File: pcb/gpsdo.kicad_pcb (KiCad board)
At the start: 4 copper layers, 140 x 100 mm, 163 parts, among them IC1 ICE40LP384-SG32, J1 JTAG, J10 CLK0, J11 CLK7, J12 USB_B_Micro, J13 CLK6, J14 CLK5, J15 CLK4, J16 RF_Shield_One_Piece, J2 SSD1306, J3 EXT_CLOCK, J4 GPS_ANT, J5 USB_B_Micro, J6 CLK3, J7 Screw_Terminal_01x03, J8 CLK2, J9 CLK1, M1 E73-2G4M08S1C-52840, Q1 S9018, SW1 EC11, SW2 MCML4-112B, U1 MCP9808_MSOP, U2 MCP9808_MSOP, U3 TPS652510, U4 LT1763xS8, U5 74LVC1G17, U6 Si5351C-B-GM, U7 74LVC1G17, U8 uBlox NEO-7M, U9 AD5761R, Y1 32768, Y2 8663-XS

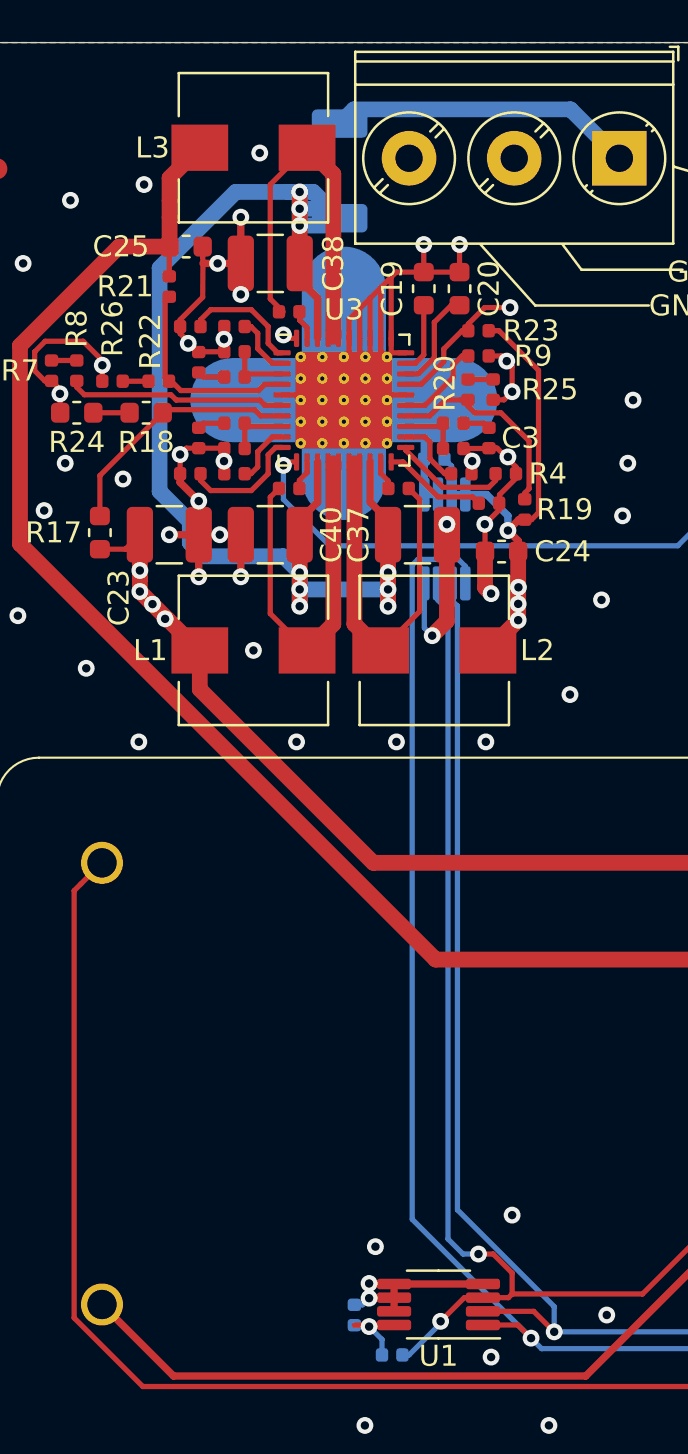
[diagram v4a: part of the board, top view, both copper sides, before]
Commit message: fix L3 to decrease ripple on 1V2 rail
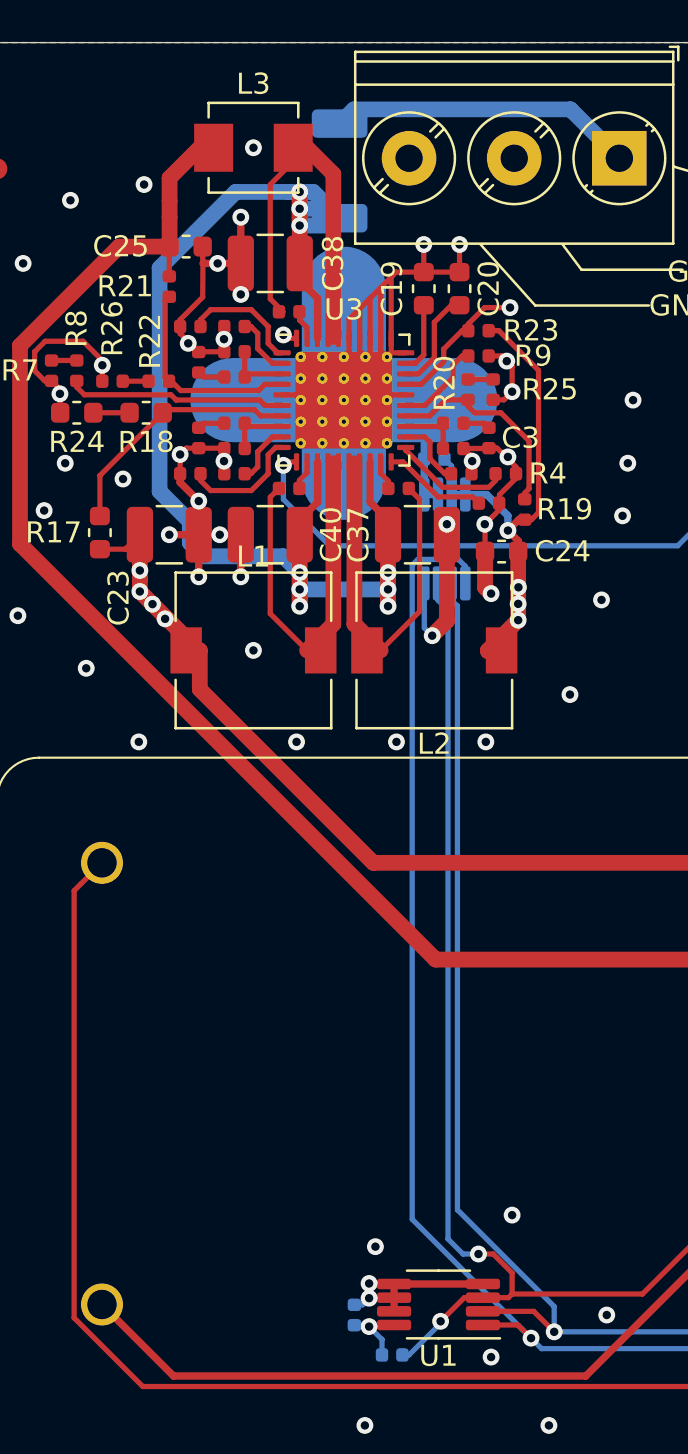
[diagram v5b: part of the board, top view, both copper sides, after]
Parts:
- L1, L2: footprint Inductor_SMD:L_Wuerth_HCI-7050 -> Inductor_SMD:L_7.3x7.3_H4.5
- L3: value 4u7 -> 220u; footprint Inductor_SMD:L_Wuerth_HCI-7050 -> Inductor_SMD:L_Vishay_IHLP-1616
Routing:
- net +3V3: track 79.4 -> 78.7 mm

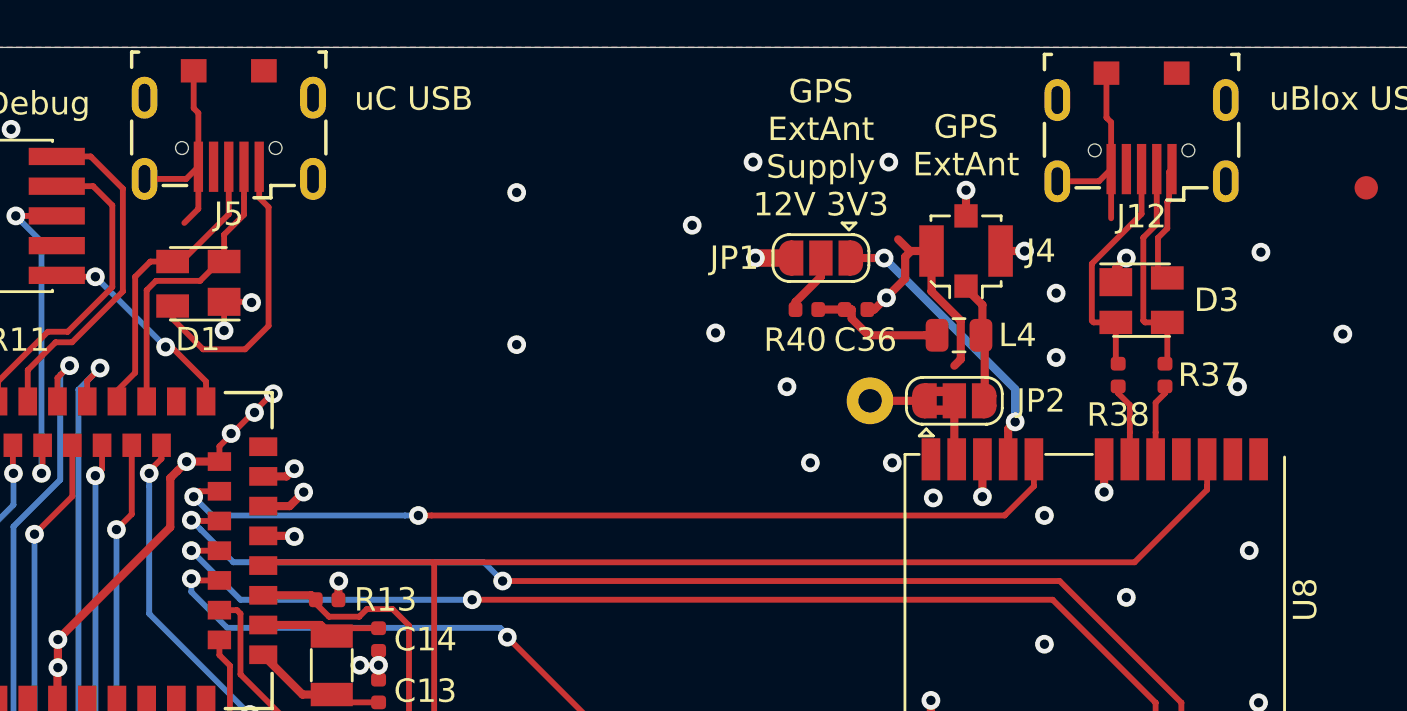
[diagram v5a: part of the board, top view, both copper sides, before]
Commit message: change GPS antenna to support either ceramic antenna or SMA with optional bias
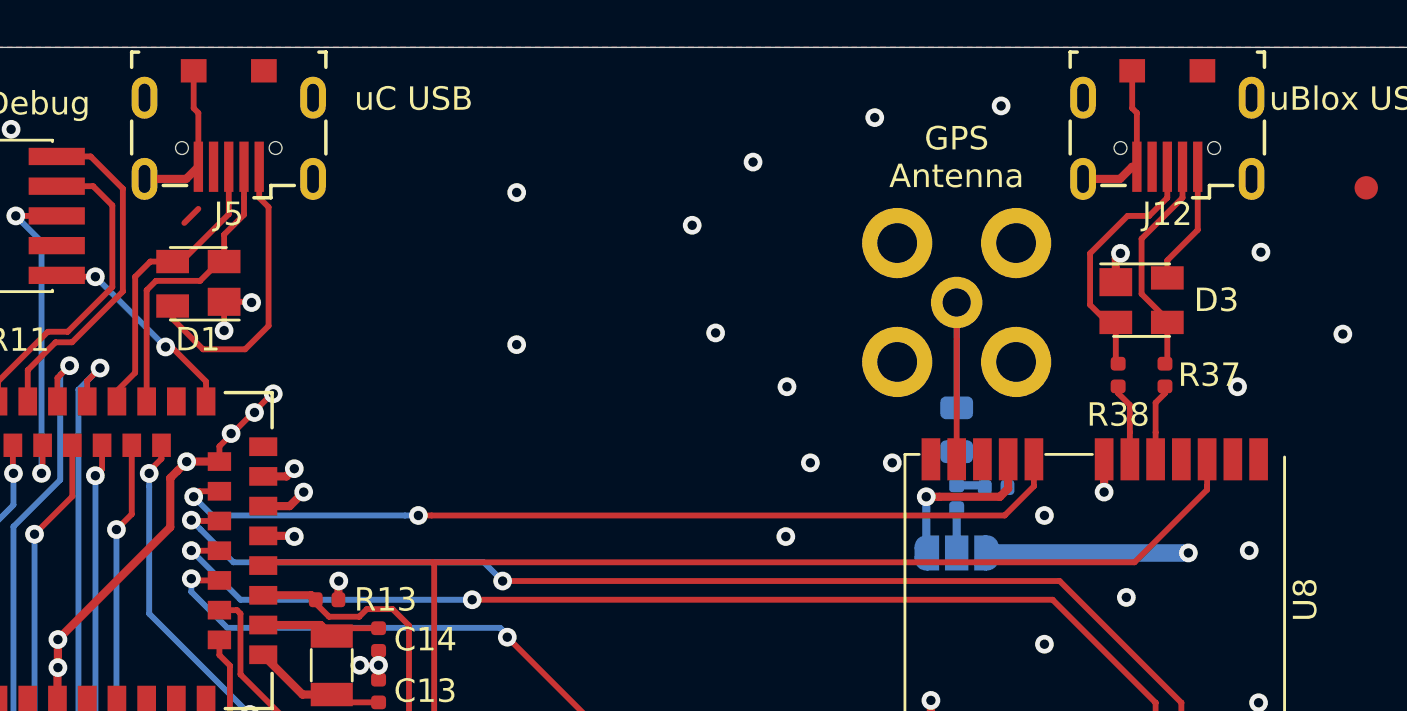
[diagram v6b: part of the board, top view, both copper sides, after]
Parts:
- removed J4: GPS_ANT, Connector_Coaxial:U.FL_Molex_MCRF_73412-0110_Vertical
- removed JP2: ANT_SEL, Jumper:SolderJumper-3_P1.3mm_Bridged2Bar12_RoundedPad1.0x1.5mm
- AE1: value 1575R-A D -> Antenna_Shield
- C36, JP1, L4, R40: moved to B.Cu
- moved JP1 13.9 mm to (139.5, 61.6), turned to 0 degrees
- moved R40 10.2 mm to (139.5, 59.2), turned to 270 degrees
- moved C36 9.67 mm to (141.2, 58.8)
- moved AE1 5.60 mm to (139.5, 50.9)
- moved L4 4.04 mm to (139.5, 56.3), turned to 270 degrees
- moved J12 1.10 mm to (148.5, 43.5)
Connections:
- L4 pad 1: /GPS_EXT_RF -> Net-(AE1-Pad1)
- U8 pad 11: Net-(JP2-Pad2) -> Net-(AE1-Pad1)
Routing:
- net +12V: track 201.5 -> 176.3 mm
- net GND: track 449.6 -> 431.5 mm, vias 225 -> 220
- net Net-(AE1-Pad1): track 2.30 -> 11.2 mm
- net /GPS_EXT_RF: track 5.28 -> 0.00 mm
- net /GPS_VCC_RF: track 12.4 -> 7.29 mm, vias 2 -> 1
- net Net-(C36-Pad1): track 5.76 -> 2.68 mm
- net Net-(JP2-Pad2): track 2.54 -> 0.00 mm
- net /GPS_USB_D+: track 10.2 -> 11.0 mm
- net Net-(JP1-Pad2): track 2.65 -> 1.91 mm
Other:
- board text added: "EXT ANT BIAS 12V 3V3"
- board text added: "GPS Antenna"
- board text removed: "GPS ExtAnt"
- board text removed: "GPS ExtAnt Supply 12V 3V3"

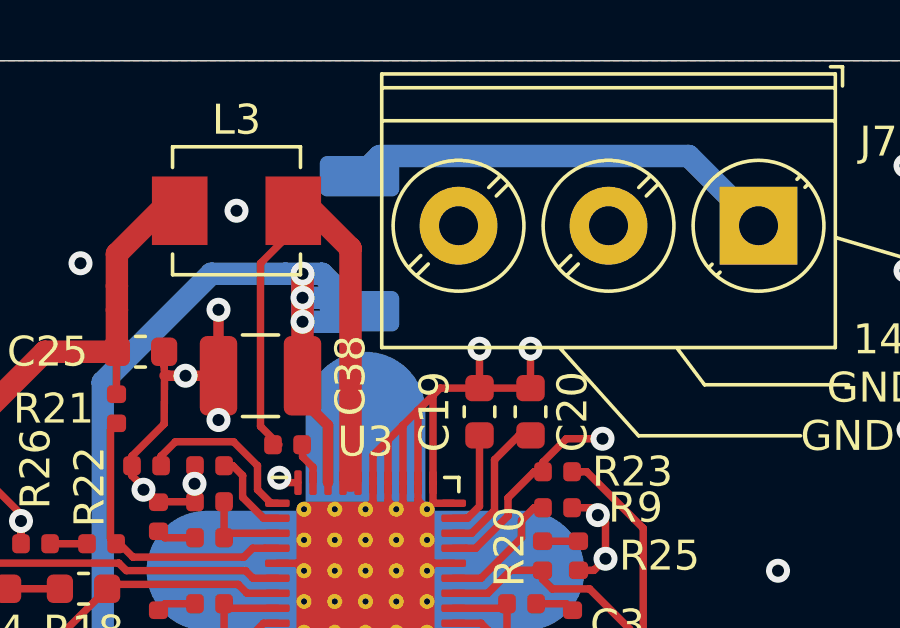
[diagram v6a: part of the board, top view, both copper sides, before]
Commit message: increase distance between input protection diode and GND pin of input connector
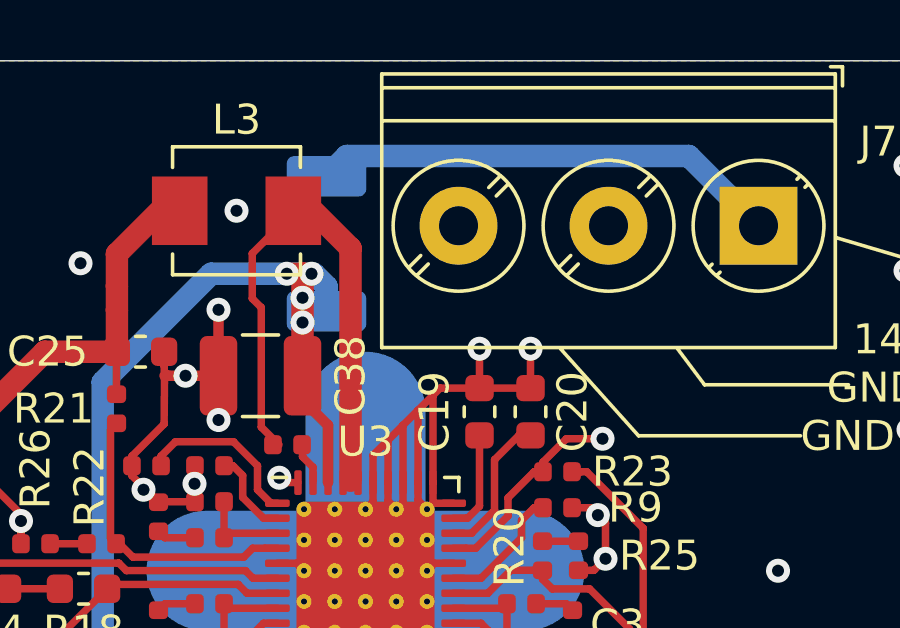
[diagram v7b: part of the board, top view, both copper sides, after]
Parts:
- moved D13 1.10 mm to (58.2, 46.1)
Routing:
- net +15V: track 75.9 -> 71.2 mm, vias 9 -> 10
- net Net-(D13-Pad2): track 14.5 -> 15.6 mm
- net Net-(C18-Pad1): track 18.3 -> 18.9 mm
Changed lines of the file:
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@@
     (thickness 1.6)
     (drawings 38)
-    (tracks 1927)
+    (tracks 1928)
     (zones 0)
     (modules 161)
@@
   )
   (setup
-    (last_trace_width 0.35)
+    (last_trace_width 0.75)
     (user_trace_width 0.35)
     (user_trace_width 0.75)
@@
   )
   (module Diode_SMD:D_2010_5025Metric (layer B.Cu)
-    (at 59.3 46.1 90)
+    (at 58.2 46.1 90)
     (descr "Diode SMD 2010 (5025 Metric), square (rectangular) end terminal, IPC_7351 nominal, (Body size source: http://www.tortai-tech.com/upload/download/2011102023233369053.pdf), generated with kicad-footprint-generator")
     (tags diode)
@@
   (segment (start 59 46.25) (end 57.75 45) (width 0.75) (layer F.Cu) (net 22) (status 20))
   (segment (start 58.999999 54) (end 59 46.25) (width 0.75) (layer F.Cu) (net 22))
-  (segment (start 56 46.750002) (end 57.75 45) (width 0.25) (layer F.Cu) (net 22) (status 20))
-  (segment (start 56.615 52.8) (end 56 52.185) (width 0.25) (layer F.Cu) (net 22) (status 10))
-  (segment (start 56 52.185) (end 56 46.750002) (width 0.25) (layer F.Cu) (net 22))
+  (segment (start 55.724998 46.425002) (end 57.15 45) (width 0.25) (layer F.Cu) (net 22))
+  (segment (start 57.15 45) (end 57.75 45) (width 0.25) (layer F.Cu) (net 22))
+  (segment (start 56.025 52.21) (end 56.025 48.225) (width 0.25) (layer F.Cu) (net 22))
+  (segment (start 56.615 52.8) (end 56.025 52.21) (width 0.25) (layer F.Cu) (net 22))
+  (segment (start 55.724998 47.924998) (end 56.025 48.225) (width 0.25) (layer F.Cu) (net 22))
+  (segment (start 55.724998 46.425002) (end 55.724998 47.924998) (width 0.25) (layer F.Cu) (net 22))
   (segment (start 62.898022 55.25) (end 62.85 55.25) (width 0.25) (layer F.Cu) (net 23))
   (segment (start 62.85 55.25) (end 62.437499 55.25) (width 0.25) (layer F.Cu) (net 23) (status 20))
@@
   (segment (start 58.25 54.0625) (end 58.25 52.15) (width 0.35) (layer F.Cu) (net 35) (status 10))
   (segment (start 58.25 52.15) (end 57.4 51.3) (width 0.35) (layer F.Cu) (net 35) (status 20))
-  (via (at 57.4 48.7) (size 0.8) (drill 0.4) (layers F.Cu B.Cu) (net 35))
   (segment (start 57.4 50.500002) (end 57.4 48.7) (width 0.35) (layer F.Cu) (net 35) (status 10))
-  (via (at 57.4 47.9) (size 0.8) (drill 0.4) (layers F.Cu B.Cu) (net 35))
   (segment (start 57.4 48.7) (end 57.4 47.9) (width 0.35) (layer F.Cu) (net 35))
-  (via (at 57.399999 47.1) (size 0.8) (drill 0.4) (layers F.Cu B.Cu) (net 35))
+  (via (at 56.875 47.1) (size 0.8) (drill 0.4) (layers F.Cu B.Cu) (net 35))
   (segment (start 57.4 47.9) (end 57.399999 47.1) (width 0.35) (layer F.Cu) (net 35))
   (via (at 57.4 65.200001) (size 0.8) (drill 0.4) (layers F.Cu B.Cu) (net 35))
@@
   (segment (start 61.599999 63.4) (end 61.6 66.800002) (width 0.75) (layer F.Cu) (net 35) (status 10))
   (segment (start 57.4 50.500002) (end 57.399999 47.1) (width 0.75) (layer F.Cu) (net 35) (status 10))
-  (segment (start 57.4 48.7) (end 57.399999 47.1) (width 0.75) (layer B.Cu) (net 35))
   (segment (start 57.4 66.799999) (end 57.4 65.200001) (width 0.75) (layer B.Cu) (net 35))
   (segment (start 61.6 65.2) (end 61.6 66.800002) (width 0.75) (layer B.Cu) (net 35))
   (segment (start 57.4 66) (end 61.6 65.999999) (width 0.75) (layer B.Cu) (net 35))
   (segment (start 61.6 65.999999) (end 61.6 66.800002) (width 0.75) (layer B.Cu) (net 35))
-  (segment (start 54.356999 47.1) (end 56.834314 47.1) (width 0.75) (layer B.Cu) (net 35))
+  (segment (start 57.399999 47.1) (end 57.375 47.1) (width 0.75) (layer F.Cu) (net 35))
+  (via (at 57.4 48.725) (size 0.8) (drill 0.4) (layers F.Cu B.Cu) (net 35))
+  (segment (start 58.2 48.35) (end 57.4 48.35) (width 0.25) (layer B.Cu) (net 35))
+  (via (at 57.7 47.1) (size 0.8) (drill 0.4) (layers F.Cu B.Cu) (net 35))
+  (segment (start 57.775 47.1) (end 58.2 47.525) (width 0.75) (layer B.Cu) (net 35))
   (segment (start 50.739999 50.717) (end 54.356999 47.1) (width 0.75) (layer B.Cu) (net 35))
   (segment (start 50.739999 61.339999) (end 50.739999 50.717) (width 0.75) (layer B.Cu) (net 35))
-  (segment (start 52.175001 63.775001) (end 52.175001 62.775001) (width 0.75) (layer B.Cu) (net 35))
-  (segment (start 56.834314 47.1) (end 57.399999 47.1) (width 0.75) (layer B.Cu) (net 35))
-  (segment (start 52.175001 62.775001) (end 50.739999 61.339999) (width 0.75) (layer B.Cu) (net 35))
+  (segment (start 57.4 65.200001) (end 56.624997 64.424998) (width 0.75) (layer B.Cu) (net 35))
   (segment (start 52.824998 64.424998) (end 52.175001 63.775001) (width 0.75) (layer B.Cu) (net 35))
+  (segment (start 52.175001 63.775001) (end 52.175001 62.775001) (width 0.75) (layer B.Cu) (net 35))
+  (segment (start 54.356999 47.1) (end 57.775 47.1) (width 0.75) (layer B.Cu) (net 35))
   (segment (start 56.624997 64.424998) (end 52.824998 64.424998) (width 0.75) (layer B.Cu) (net 35))
-  (segment (start 57.4 65.200001) (end 56.624997 64.424998) (width 0.75) (layer B.Cu) (net 35))
-  (segment (start 58.95 48.7) (end 59.3 48.35) (width 0.75) (layer B.Cu) (net 35) (status 30))
-  (segment (start 57.4 48.7) (end 58.95 48.7) (width 0.75) (layer B.Cu) (net 35) (status 20))
-  (segment (start 58.85 47.9) (end 59.3 48.35) (width 0.75) (layer B.Cu) (net 35) (status 30))
-  (segment (start 57.4 47.9) (end 58.85 47.9) (width 0.75) (layer B.Cu) (net 35) (status 20))
-  (segment (start 58.05 47.1) (end 59.3 48.35) (width 0.75) (layer B.Cu) (net 35) (status 20))
-  (segment (start 57.399999 47.1) (end 58.05 47.1) (width 0.75) (layer B.Cu) (net 35))
+  (segment (start 52.175001 62.775001) (end 50.739999 61.339999) (width 0.75) (layer B.Cu) (net 35))
+  (segment (start 58.2 47.525) (end 58.2 48.35) (width 0.75) (layer B.Cu) (net 35))
+  (segment (start 56.875 47.1) (end 57.7 47.1) (width 0.75) (layer F.Cu) (net 35))
+  (via (at 57.4 47.9) (size 0.8) (drill 0.4) (layers F.Cu B.Cu) (net 35))
   (segment (start 92.524999 79.475001) (end 92.6 79.4) (width 0.35) (layer F.Cu) (net 36) (status 30))
   (segment (start 92.524999 81.15) (end 92.524999 79.475001) (width 0.35) (layer F.Cu) (net 36) (status 30))
@@
   (segment (start 120.4 128.8) (end 112.11251 128.80001) (width 0.25) (layer F.Cu) (net 52))
   (segment (start 111.7875 128.475) (end 111.7875 128) (width 0.25) (layer F.Cu) (net 52) (status 20))
-  (segment (start 59.975 43.175) (end 59.3 43.85) (width 0.75) (layer B.Cu) (net 53) (status 30))
-  (segment (start 72.6 45.5) (end 70.275 43.175) (width 0.75) (layer B.Cu) (net 53) (status 10))
-  (segment (start 70.275 43.175) (end 59.975 43.175) (width 0.75) (layer B.Cu) (net 53) (status 20))
+  (segment (start 58.875 43.175) (end 58.2 43.85) (width 0.75) (layer B.Cu) (net 53))
+  (segment (start 72.6 45.5) (end 70.275 43.175) (width 0.75) (layer B.Cu) (net 53))
+  (segment (start 70.275 43.175) (end 58.875 43.175) (width 0.75) (layer B.Cu) (net 53))
   (segment (start 124.685 118.6975) (end 124.685 119.7) (width 0.25) (layer F.Cu) (net 54) (status 20))
   (segment (start 123.9875 118) (end 124.685 118.6975) (width 0.25) (layer F.Cu) (net 54) (status 10))
